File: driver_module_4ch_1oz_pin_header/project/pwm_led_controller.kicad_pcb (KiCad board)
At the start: 2 copper layers, 40 x 42 mm, 37 parts, among them J1 Conn_01x05_Male, J2 Conn_01x02_Male, J3 Conn_01x02_Male, J4 Conn_01x02_Male, J5 Conn_01x02_Male, J6 Conn_01x02_Male, J7 Conn_01x02_Male, U1 AL8843, U2 AL8843, U3 AL8843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

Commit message: Проект выполнен под установку светильника
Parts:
- J2, J3: value Conn_01x02_Male -> Conn_01x04_Male; footprint Connector_PinHeader_2.54mm:PinHeader_1x06_P2.54mm_Vertical -> Connector_PinHeader_2.54mm:PinHeader_1x04_P2.54mm_Vertical
- moved J4 6.62 mm to (132.5, 53.0), turned to 270 degrees
- moved J5 4.51 mm to (133.5, 66.0), turned to 270 degrees
- moved J3 3.21 mm to (137.2, 83.0)
- moved J6 2.52 mm to (133.5, 79.0), turned to 270 degrees
- moved R5 2.50 mm to (122.5, 57.5)
- moved R6 2.50 mm to (122.5, 68.0)
- moved R7 2.50 mm to (122.5, 78.5)
- moved R8 2.50 mm to (122.5, 89.0)
- moved J7 1.00 mm to (132.5, 91.0), turned to 270 degrees
- moved J2 0.56 mm to (137.2, 57.5)
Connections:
- J2 pad 2: GND -> +15V
- J2 pad 3: (no net) -> GND
- J2 pad 4: (no net) -> GND
- J3 pad 2: GND -> +28V
- J3 pad 3: (no net) -> GND
- J3 pad 4: (no net) -> GND
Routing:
- net /Set_3: track 36.8 -> 68.7 mm
- net +28V: track 58.5 -> 63.8 mm
- net /Led_1-: track 5.36 -> 9.12 mm
- net /Led_0-: track 5.36 -> 6.64 mm
- net /Set_1: track 37.2 -> 36.4 mm, vias 0 -> 1
- net /Led_2-: track 5.36 -> 6.11 mm
- net /Led_3-: track 5.36 -> 6.05 mm
- net /Set_0: track 37.2 -> 36.6 mm, vias 0 -> 1
- net /Set_2: track 37.2 -> 37.6 mm, vias 0 -> 1
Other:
- board text added: "PWR Input"

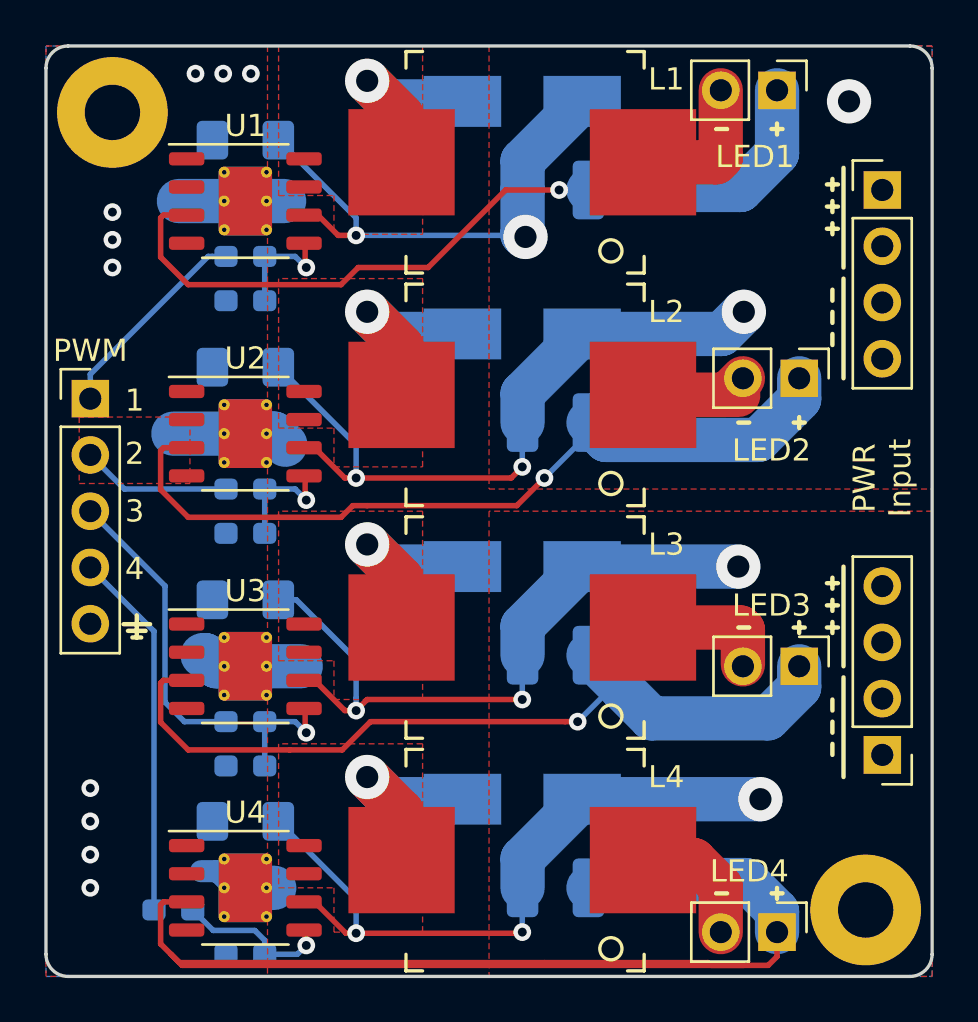
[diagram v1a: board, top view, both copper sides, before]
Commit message: Подогнал расположение вилок под светодиодную плату
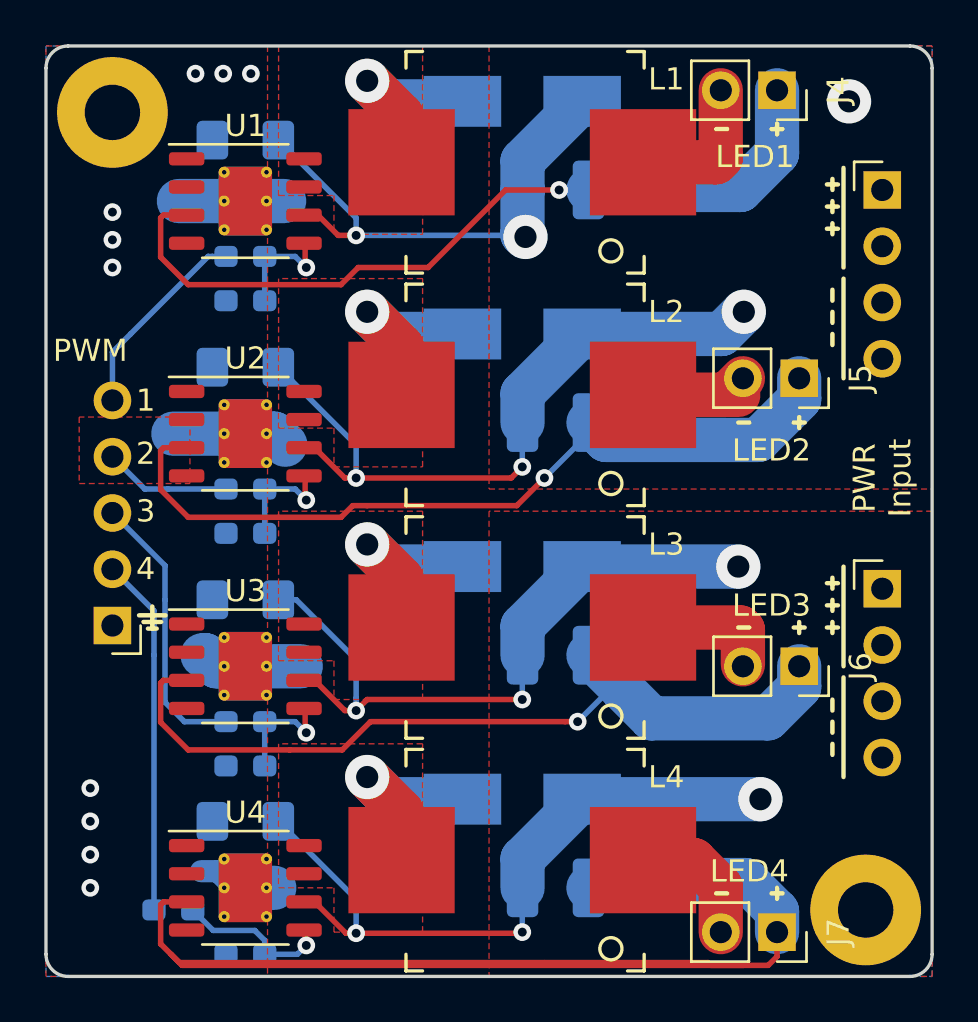
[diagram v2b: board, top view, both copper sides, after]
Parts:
- J1: footprint Connector_PinHeader_2.54mm:PinHeader_1x05_P2.54mm_Vertical -> my_lib:PinHeader_1x05_P2.54mm_Horizontal
- J2, J3: footprint Connector_PinHeader_2.54mm:PinHeader_1x04_P2.54mm_Vertical -> my_lib:PinHeader_1x04_P2.54mm_Horizontal
- J4, J5, J6, J7: footprint Connector_PinHeader_2.54mm:PinHeader_1x02_P2.54mm_Vertical -> Connector_PinSocket_2.54mm:PinSocket_1x02_P2.54mm_Vertical
- moved J1 10.3 mm to (102.5, 77.2), turned to 180 degrees
- moved J3 7.50 mm to (137.2, 75.5), turned to 0 degrees
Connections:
- J1 pad 1: /PWM_1 -> GND
- J1 pad 2: /PWM_2 -> /PWM_4
- J1 pad 4: /PWM_4 -> /PWM_2
- J1 pad 5: GND -> /PWM_1
- J3 pad 1: +28V -> GND
- J3 pad 2: +28V -> GND
- J3 pad 3: GND -> +28V
- J3 pad 4: GND -> +28V
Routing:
- net /PWM_2: track 6.76 -> 5.73 mm
